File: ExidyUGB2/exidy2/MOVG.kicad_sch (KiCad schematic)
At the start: 17 parts, among them U11D M2708, U11F_ 74LS04, U12D 74LS166, U13D 74LS166, U14A 74LS157, U14D 74LS166, U14E 74LS157, U14H TBP18S030, U15C_ 74LS00, U15D 74LS166, U15H 74LS00, U15H_ 74LS00, U16H 74LS139, U2F_ 74LS20

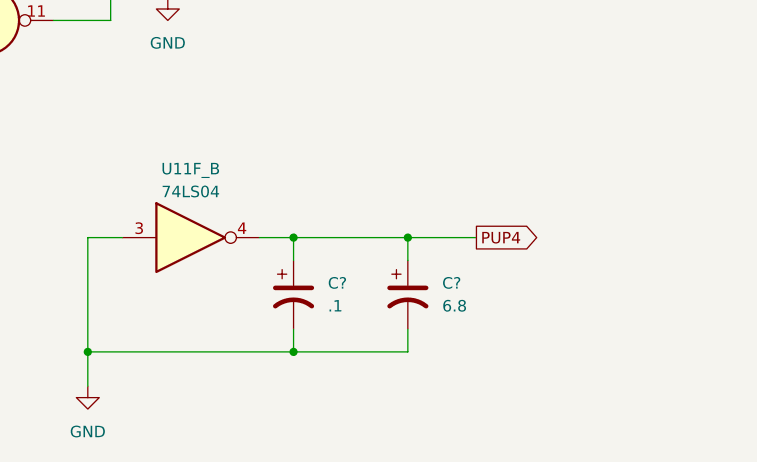
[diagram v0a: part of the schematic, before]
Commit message: Updates to KiCAD8
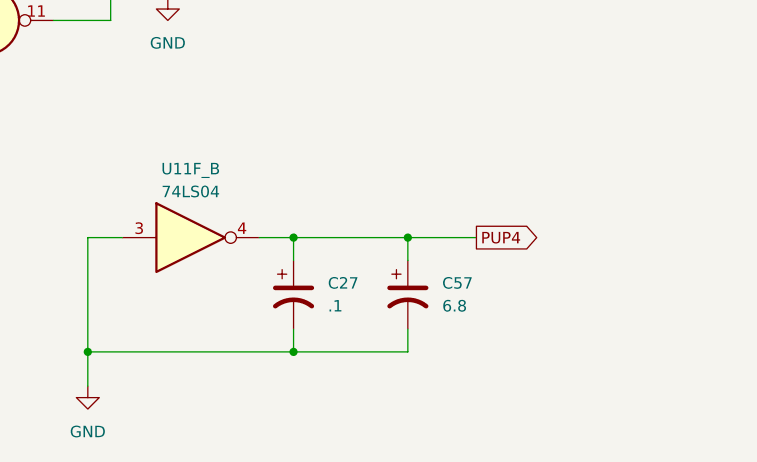
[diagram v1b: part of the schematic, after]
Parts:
- gave numbers to parts that had none: 2
